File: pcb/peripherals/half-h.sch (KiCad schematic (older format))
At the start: 12 parts, among them Q201 RQ3E100BNTB, Q202 RQ3E100BNTB, U201 DGD0506A

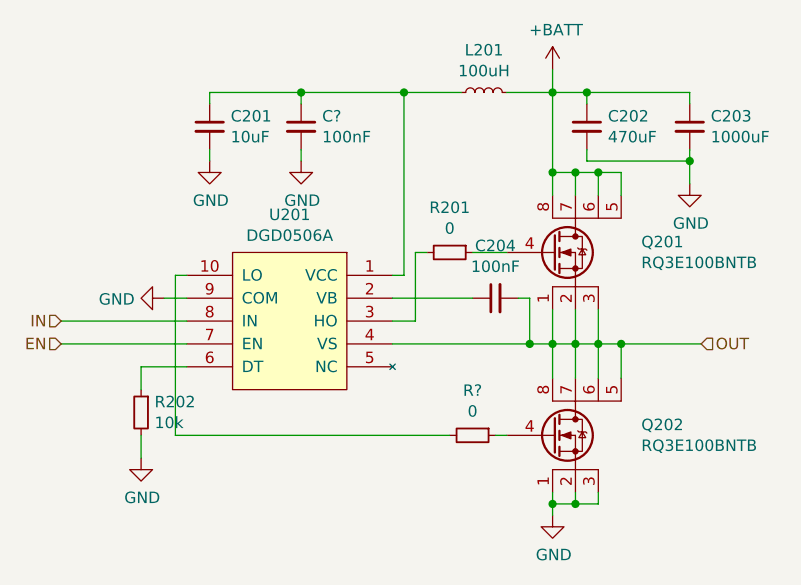
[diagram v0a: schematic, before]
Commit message: Schematic done; TODO add footprints for connectors
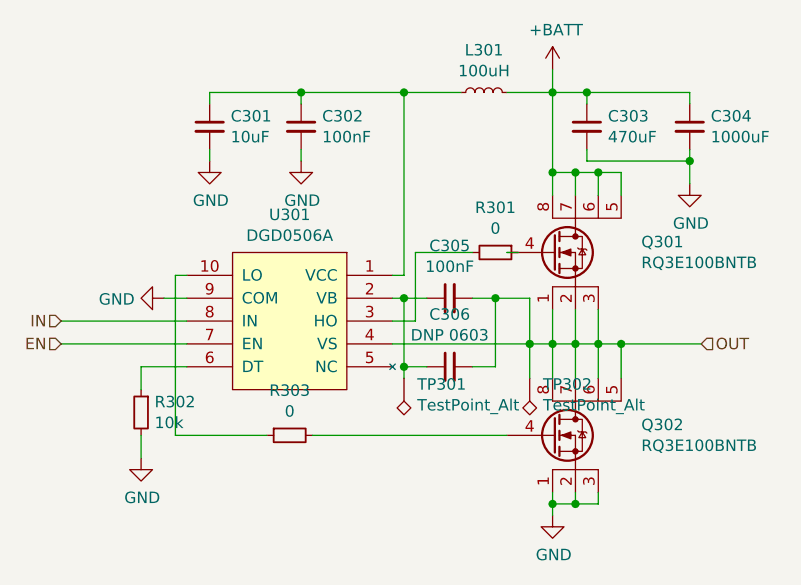
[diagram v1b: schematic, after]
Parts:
- added C206: DNP 0603, Capacitors_SMD:C_0603_HandSoldering, symbol Device:C_Small
- added TP201, TP202: TestPoint_Alt, symbol Connector:TestPoint_Alt
- C205: renamed from C204; footprint (none) -> Capacitors_SMD:C_0402; Mouser (none) -> 710-885012105018
- gave numbers to parts that had none: 2
- renumbered C202 to C203, C203 to C204
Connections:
- net OUT: now also C206.2, TP202.1
- net at U201.10 (LO): now also R203.1; no longer R203.2
- net at C205.1, U201.2 (VB): now also C206.1, TP201.1
- net at Q202.4 (G): now also R203.2; no longer R203.1
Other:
- moved on the sheet: C305, R301, R303

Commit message: Save before autofill
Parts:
- TP201: footprint (none) -> Measurement_Points:Measurement_Point_Round-SMD-Pad_Small; Mouser (none) -> NoPart
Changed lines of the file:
@@
 $Descr A4 11693 8268
 encoding utf-8
-Sheet 3 9
+Sheet 2 9
 Title ""
 Date ""
@@
 AR Path="/5B6E6A6C/5B7233C9" Ref="Q801"  Part="1"
 AR Path="/5B6E6A71/5B7233C9" Ref="Q901"  Part="1"
-F 0 "Q301" H 5788 3146 50  0000 L CNN
+F 0 "Q201" H 5788 3146 50  0000 L CNN
 F 1 "RQ3E100BNTB" H 5788 3055 50  0000 L CNN
 F 2 "peripherals:Rohm-HSMT8" H 5600 3200 50  0001 C CNN
@@
 AR Path="/5B6E6A6C/5B7233D1" Ref="U801"  Part="1"
 AR Path="/5B6E6A71/5B7233D1" Ref="U901"  Part="1"
-F 0 "U301" H 4250 3865 50  0000 C CNN
+F 0 "U201" H 4250 3865 50  0000 C CNN
 F 1 "DGD0506A" H 4250 3774 50  0000 C CNN
 F 2 "peripherals:Diodes-MSOP10" H 4250 3800 50  0001 C CNN
@@
 AR Path="/5B6E6A6C/5B7233E5" Ref="#PWR0807"  Part="1"
 AR Path="/5B6E6A71/5B7233E5" Ref="#PWR0907"  Part="1"
-F 0 "#PWR0307" H 5400 4000 50  0001 C CNN
+F 0 "#PWR0207" H 5400 4000 50  0001 C CNN
 F 1 "GND" H 5405 4077 50  0000 C CNN
 F 2 "" H 5400 4250 50  0001 C CNN
@@
 AR Path="/5B6E6A6C/5B7233F3" Ref="R801"  Part="1"
 AR Path="/5B6E6A71/5B7233F3" Ref="R901"  Part="1"
-F 0 "R301" V 4954 3100 50  0000 C CNN
+F 0 "R201" V 4954 3100 50  0000 C CNN
 F 1 "0" V 5045 3100 50  0000 C CNN
 F 2 "Resistors_SMD:R_0603_HandSoldering" H 5150 3100 50  0001 C CNN
@@
 AR Path="/5B6E6A6C/5B723403" Ref="#PWR0805"  Part="1"
 AR Path="/5B6E6A71/5B723403" Ref="#PWR0905"  Part="1"
-F 0 "#PWR0305" H 3700 3050 50  0001 C CNN
+F 0 "#PWR0205" H 3700 3050 50  0001 C CNN
 F 1 "GND" V 3705 3172 50  0000 R CNN
 F 2 "" H 3700 3300 50  0001 C CNN
@@
 AR Path="/5B6E6A6C/5B723409" Ref="R802"  Part="1"
 AR Path="/5B6E6A71/5B723409" Ref="R902"  Part="1"
-F 0 "R302" H 3541 3846 50  0000 R CNN
+F 0 "R202" H 3541 3846 50  0000 R CNN
 F 1 "10k" H 3541 3755 50  0000 R CNN
 F 2 "Resistors_SMD:R_0402" H 3600 3800 50  0001 C CNN
@@
 AR Path="/5B6E6A6C/5B723410" Ref="#PWR0806"  Part="1"
 AR Path="/5B6E6A71/5B723410" Ref="#PWR0906"  Part="1"
-F 0 "#PWR0306" H 3600 3750 50  0001 C CNN
+F 0 "#PWR0206" H 3600 3750 50  0001 C CNN
 F 1 "GND" H 3605 3827 50  0000 C CNN
 F 2 "" H 3600 4000 50  0001 C CNN
@@
 AR Path="/5B6E6A6C/5B723429" Ref="C805"  Part="1"
 AR Path="/5B6E6A71/5B723429" Ref="C905"  Part="1"
-F 0 "C305" V 4721 3300 50  0000 C CNN
+F 0 "C205" V 4721 3300 50  0000 C CNN
 F 1 "100nF" V 4812 3300 50  0000 C CNN
 F 2 "Capacitors_SMD:C_0402" H 4950 3300 50  0001 C CNN
@@
 AR Path="/5B6E6A6C/5B723443" Ref="C801"  Part="1"
 AR Path="/5B6E6A71/5B723443" Ref="C901"  Part="1"
-F 0 "C301" H 3992 2596 50  0000 L CNN
+F 0 "C201" H 3992 2596 50  0000 L CNN
 F 1 "10uF" H 3992 2505 50  0000 L CNN
 F 2 "Capacitors_SMD:CP_Elec_4x5.7" H 3900 2550 50  0001 C CNN
@@
 AR Path="/5B6E6A6C/5B72344C" Ref="#PWR0803"  Part="1"
 AR Path="/5B6E6A71/5B72344C" Ref="#PWR0903"  Part="1"
-F 0 "#PWR0303" H 4300 2450 50  0001 C CNN
+F 0 "#PWR0203" H 4300 2450 50  0001 C CNN
 F 1 "GND" H 4305 2527 50  0000 C CNN
 F 2 "" H 4300 2700 50  0001 C CNN
@@
 AR Path="/5B6E6A6C/5B723454" Ref="C803"  Part="1"
 AR Path="/5B6E6A71/5B723454" Ref="C903"  Part="1"
-F 0 "C303" H 5642 2596 50  0000 L CNN
+F 0 "C203" H 5642 2596 50  0000 L CNN
 F 1 "470uF" H 5642 2505 50  0000 L CNN
 F 2 "Capacitors_ThroughHole:CP_Radial_D10.0mm_P5.00mm" H 5550 2550 50  0001 C CNN
@@
 AR Path="/5B6E6A6C/5B72345C" Ref="C804"  Part="1"
 AR Path="/5B6E6A71/5B72345C" Ref="C904"  Part="1"
-F 0 "C304" H 6092 2596 50  0000 L CNN
+F 0 "C204" H 6092 2596 50  0000 L CNN
 F 1 "1000uF" H 6092 2505 50  0000 L CNN
 F 2 "Capacitors_ThroughHole:CP_Radial_D18.0mm_P7.50mm" H 6000 2550 50  0001 C CNN
@@
 AR Path="/5B6E6A6C/5B723466" Ref="#PWR0804"  Part="1"
 AR Path="/5B6E6A71/5B723466" Ref="#PWR0904"  Part="1"
-F 0 "#PWR0304" H 6000 2550 50  0001 C CNN
+F 0 "#PWR0204" H 6000 2550 50  0001 C CNN
 F 1 "GND" H 6005 2627 50  0000 C CNN
 F 2 "" H 6000 2800 50  0001 C CNN
@@
 AR Path="/5B6E6A6C/5B723472" Ref="L801"  Part="1"
 AR Path="/5B6E6A71/5B723472" Ref="L901"  Part="1"
-F 0 "L301" V 5285 2400 50  0000 C CNN
+F 0 "L201" V 5285 2400 50  0000 C CNN
 F 1 "100uH" V 5194 2400 50  0000 C CNN
 F 2 "Resistors_SMD:R_0805_HandSoldering" H 5100 2400 50  0001 C CNN
@@
 AR Path="/5B6E6A6C/5B72347E" Ref="#PWR0801"  Part="1"
 AR Path="/5B6E6A71/5B72347E" Ref="#PWR0901"  Part="1"
-F 0 "#PWR0301" H 5400 2150 50  0001 C CNN
+F 0 "#PWR0201" H 5400 2150 50  0001 C CNN
 F 1 "+BATT" H 5415 2473 50  0000 C CNN
 F 2 "" H 5400 2300 50  0001 C CNN
@@
 AR Path="/5B6E6A6C/5B723489" Ref="Q802"  Part="1"
 AR Path="/5B6E6A71/5B723489" Ref="Q902"  Part="1"
-F 0 "Q302" H 5788 3946 50  0000 L CNN
+F 0 "Q202" H 5788 3946 50  0000 L CNN
 F 1 "RQ3E100BNTB" H 5788 3855 50  0000 L CNN
 F 2 "peripherals:Rohm-HSMT8" H 5600 4000 50  0001 C CNN
@@
 AR Path="/5B6E6A6C/5B727333" Ref="R803"  Part="1"
 AR Path="/5B6E6A71/5B727333" Ref="R903"  Part="1"
-F 0 "R303" V 4054 3900 50  0000 C CNN
+F 0 "R203" V 4054 3900 50  0000 C CNN
 F 1 "0" V 4145 3900 50  0000 C CNN
 F 2 "Resistors_SMD:R_0603_HandSoldering" H 4250 3900 50  0001 C CNN
@@
 AR Path="/5B6E6A6C/5B728A25" Ref="#PWR0802"  Part="1"
 AR Path="/5B6E6A71/5B728A25" Ref="#PWR0902"  Part="1"
-F 0 "#PWR0302" H 3900 2450 50  0001 C CNN
+F 0 "#PWR0202" H 3900 2450 50  0001 C CNN
 F 1 "GND" H 3905 2527 50  0000 C CNN
 F 2 "" H 3900 2700 50  0001 C CNN
@@
 AR Path="/5B6E6A6C/5B72F72D" Ref="C802"  Part="1"
 AR Path="/5B6E6A71/5B72F72D" Ref="C902"  Part="1"
-F 0 "C302" H 4392 2596 50  0000 L CNN
+F 0 "C202" H 4392 2596 50  0000 L CNN
 F 1 "100nF" H 4392 2505 50  0000 L CNN
 F 2 "Capacitors_SMD:C_0402" H 4300 2550 50  0001 C CNN
@@
 AR Path="/5B6E6A6C/5B6EFABB" Ref="C806"  Part="1"
 AR Path="/5B6E6A71/5B6EFABB" Ref="C906"  Part="1"
-F 0 "C306" V 4721 3600 50  0000 C CNN
+F 0 "C206" V 4721 3600 50  0000 C CNN
 F 1 "DNP 0603" V 4812 3600 50  0000 C CNN
 F 2 "Capacitors_SMD:C_0603_HandSoldering" H 4950 3600 50  0001 C CNN
@@
 AR Path="/5B6E6A6C/5B6F8326" Ref="TP801"  Part="1"
 AR Path="/5B6E6A71/5B6F8326" Ref="TP901"  Part="1"
-F 0 "TP301" H 4692 3677 50  0000 R CNN
+F 0 "TP201" H 4692 3677 50  0000 R CNN
 F 1 "TestPoint_Alt" H 4692 3768 50  0000 R CNN
-F 2 "" H 4950 3650 50  0001 C CNN
+F 2 "Measurement_Points:Measurement_Point_Round-SMD-Pad_Small" H 4950 3650 50  0001 C CNN
 F 3 "~" H 4950 3650 50  0001 C CNN
+F 4 "NoPart" H 4750 3650 50  0001 C CNN "Mouser"
 	1    4750 3650
 	-1   0    0    1
@@
 AR Path="/5B6E6A6C/5B6F99EB" Ref="TP802"  Part="1"
 AR Path="/5B6E6A71/5B6F99EB" Ref="TP902"  Part="1"
-F 0 "TP302" H 5242 3677 50  0000 R CNN
+F 0 "TP202" H 5242 3677 50  0000 R CNN
 F 1 "TestPoint_Alt" H 5242 3768 50  0000 R CNN
 F 2 "" H 5500 3650 50  0001 C CNN

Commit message: Save before messing with tiler script
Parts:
- TP202: footprint (none) -> Measurement_Points:Measurement_Point_Round-SMD-Pad_Small; Mouser (none) -> NoPart
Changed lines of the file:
@@
 AR Path="/5B6E6A6C/5B7233C9" Ref="Q801"  Part="1"
 AR Path="/5B6E6A71/5B7233C9" Ref="Q901"  Part="1"
-F 0 "Q201" H 5788 3146 50  0000 L CNN
+F 0 "Q301" H 5788 3146 50  0000 L CNN
 F 1 "RQ3E100BNTB" H 5788 3055 50  0000 L CNN
 F 2 "peripherals:Rohm-HSMT8" H 5600 3200 50  0001 C CNN
@@
 AR Path="/5B6E6A6C/5B7233D1" Ref="U801"  Part="1"
 AR Path="/5B6E6A71/5B7233D1" Ref="U901"  Part="1"
-F 0 "U201" H 4250 3865 50  0000 C CNN
+F 0 "U301" H 4250 3865 50  0000 C CNN
 F 1 "DGD0506A" H 4250 3774 50  0000 C CNN
 F 2 "peripherals:Diodes-MSOP10" H 4250 3800 50  0001 C CNN
@@
 AR Path="/5B6E6A6C/5B7233E5" Ref="#PWR0807"  Part="1"
 AR Path="/5B6E6A71/5B7233E5" Ref="#PWR0907"  Part="1"
-F 0 "#PWR0207" H 5400 4000 50  0001 C CNN
+F 0 "#PWR0307" H 5400 4000 50  0001 C CNN
 F 1 "GND" H 5405 4077 50  0000 C CNN
 F 2 "" H 5400 4250 50  0001 C CNN
@@
 AR Path="/5B6E6A6C/5B7233F3" Ref="R801"  Part="1"
 AR Path="/5B6E6A71/5B7233F3" Ref="R901"  Part="1"
-F 0 "R201" V 4954 3100 50  0000 C CNN
+F 0 "R301" V 4954 3100 50  0000 C CNN
 F 1 "0" V 5045 3100 50  0000 C CNN
 F 2 "Resistors_SMD:R_0603_HandSoldering" H 5150 3100 50  0001 C CNN
@@
 AR Path="/5B6E6A6C/5B723403" Ref="#PWR0805"  Part="1"
 AR Path="/5B6E6A71/5B723403" Ref="#PWR0905"  Part="1"
-F 0 "#PWR0205" H 3700 3050 50  0001 C CNN
+F 0 "#PWR0305" H 3700 3050 50  0001 C CNN
 F 1 "GND" V 3705 3172 50  0000 R CNN
 F 2 "" H 3700 3300 50  0001 C CNN
@@
 AR Path="/5B6E6A6C/5B723409" Ref="R802"  Part="1"
 AR Path="/5B6E6A71/5B723409" Ref="R902"  Part="1"
-F 0 "R202" H 3541 3846 50  0000 R CNN
+F 0 "R302" H 3541 3846 50  0000 R CNN
 F 1 "10k" H 3541 3755 50  0000 R CNN
 F 2 "Resistors_SMD:R_0402" H 3600 3800 50  0001 C CNN
@@
 AR Path="/5B6E6A6C/5B723410" Ref="#PWR0806"  Part="1"
 AR Path="/5B6E6A71/5B723410" Ref="#PWR0906"  Part="1"
-F 0 "#PWR0206" H 3600 3750 50  0001 C CNN
+F 0 "#PWR0306" H 3600 3750 50  0001 C CNN
 F 1 "GND" H 3605 3827 50  0000 C CNN
 F 2 "" H 3600 4000 50  0001 C CNN
@@
 AR Path="/5B6E6A6C/5B723429" Ref="C805"  Part="1"
 AR Path="/5B6E6A71/5B723429" Ref="C905"  Part="1"
-F 0 "C205" V 4721 3300 50  0000 C CNN
+F 0 "C305" V 4721 3300 50  0000 C CNN
 F 1 "100nF" V 4812 3300 50  0000 C CNN
 F 2 "Capacitors_SMD:C_0402" H 4950 3300 50  0001 C CNN
@@
 	4750 3200 4700 3200
 Wire Wire Line
-	6050 3500 5700 3500
+	6050 3500 5900 3500
 Connection ~ 5700 3500
 Wire Wire Line
@@
 AR Path="/5B6E6A6C/5B723443" Ref="C801"  Part="1"
 AR Path="/5B6E6A71/5B723443" Ref="C901"  Part="1"
-F 0 "C201" H 3992 2596 50  0000 L CNN
+F 0 "C301" H 3992 2596 50  0000 L CNN
 F 1 "10uF" H 3992 2505 50  0000 L CNN
 F 2 "Capacitors_SMD:CP_Elec_4x5.7" H 3900 2550 50  0001 C CNN
@@
 AR Path="/5B6E6A6C/5B72344C" Ref="#PWR0803"  Part="1"
 AR Path="/5B6E6A71/5B72344C" Ref="#PWR0903"  Part="1"
-F 0 "#PWR0203" H 4300 2450 50  0001 C CNN
+F 0 "#PWR0303" H 4300 2450 50  0001 C CNN
 F 1 "GND" H 4305 2527 50  0000 C CNN
 F 2 "" H 4300 2700 50  0001 C CNN
@@
 AR Path="/5B6E6A6C/5B723454" Ref="C803"  Part="1"
 AR Path="/5B6E6A71/5B723454" Ref="C903"  Part="1"
-F 0 "C203" H 5642 2596 50  0000 L CNN
+F 0 "C303" H 5642 2596 50  0000 L CNN
 F 1 "470uF" H 5642 2505 50  0000 L CNN
 F 2 "Capacitors_ThroughHole:CP_Radial_D10.0mm_P5.00mm" H 5550 2550 50  0001 C CNN
@@
 AR Path="/5B6E6A6C/5B72345C" Ref="C804"  Part="1"
 AR Path="/5B6E6A71/5B72345C" Ref="C904"  Part="1"
-F 0 "C204" H 6092 2596 50  0000 L CNN
+F 0 "C304" H 6092 2596 50  0000 L CNN
 F 1 "1000uF" H 6092 2505 50  0000 L CNN
 F 2 "Capacitors_ThroughHole:CP_Radial_D18.0mm_P7.50mm" H 6000 2550 50  0001 C CNN
@@
 AR Path="/5B6E6A6C/5B723466" Ref="#PWR0804"  Part="1"
 AR Path="/5B6E6A71/5B723466" Ref="#PWR0904"  Part="1"
-F 0 "#PWR0204" H 6000 2550 50  0001 C CNN
+F 0 "#PWR0304" H 6000 2550 50  0001 C CNN
 F 1 "GND" H 6005 2627 50  0000 C CNN
 F 2 "" H 6000 2800 50  0001 C CNN
@@
 AR Path="/5B6E6A6C/5B723472" Ref="L801"  Part="1"
 AR Path="/5B6E6A71/5B723472" Ref="L901"  Part="1"
-F 0 "L201" V 5285 2400 50  0000 C CNN
+F 0 "L301" V 5285 2400 50  0000 C CNN
 F 1 "100uH" V 5194 2400 50  0000 C CNN
 F 2 "Resistors_SMD:R_0805_HandSoldering" H 5100 2400 50  0001 C CNN
@@
 AR Path="/5B6E6A6C/5B72347E" Ref="#PWR0801"  Part="1"
 AR Path="/5B6E6A71/5B72347E" Ref="#PWR0901"  Part="1"
-F 0 "#PWR0201" H 5400 2150 50  0001 C CNN
+F 0 "#PWR0301" H 5400 2150 50  0001 C CNN
 F 1 "+BATT" H 5415 2473 50  0000 C CNN
 F 2 "" H 5400 2300 50  0001 C CNN
@@
 AR Path="/5B6E6A6C/5B723489" Ref="Q802"  Part="1"
 AR Path="/5B6E6A71/5B723489" Ref="Q902"  Part="1"
-F 0 "Q202" H 5788 3946 50  0000 L CNN
+F 0 "Q302" H 5788 3946 50  0000 L CNN
 F 1 "RQ3E100BNTB" H 5788 3855 50  0000 L CNN
 F 2 "peripherals:Rohm-HSMT8" H 5600 4000 50  0001 C CNN
@@
 AR Path="/5B6E6A6C/5B727333" Ref="R803"  Part="1"
 AR Path="/5B6E6A71/5B727333" Ref="R903"  Part="1"
-F 0 "R203" V 4054 3900 50  0000 C CNN
+F 0 "R303" V 4054 3900 50  0000 C CNN
 F 1 "0" V 4145 3900 50  0000 C CNN
 F 2 "Resistors_SMD:R_0603_HandSoldering" H 4250 3900 50  0001 C CNN
@@
 AR Path="/5B6E6A6C/5B728A25" Ref="#PWR0802"  Part="1"
 AR Path="/5B6E6A71/5B728A25" Ref="#PWR0902"  Part="1"
-F 0 "#PWR0202" H 3900 2450 50  0001 C CNN
+F 0 "#PWR0302" H 3900 2450 50  0001 C CNN
 F 1 "GND" H 3905 2527 50  0000 C CNN
 F 2 "" H 3900 2700 50  0001 C CNN
@@
 AR Path="/5B6E6A6C/5B72F72D" Ref="C802"  Part="1"
 AR Path="/5B6E6A71/5B72F72D" Ref="C902"  Part="1"
-F 0 "C202" H 4392 2596 50  0000 L CNN
+F 0 "C302" H 4392 2596 50  0000 L CNN
 F 1 "100nF" H 4392 2505 50  0000 L CNN
 F 2 "Capacitors_SMD:C_0402" H 4300 2550 50  0001 C CNN
@@
 AR Path="/5B6E6A6C/5B6EFABB" Ref="C806"  Part="1"
 AR Path="/5B6E6A71/5B6EFABB" Ref="C906"  Part="1"
-F 0 "C206" V 4721 3600 50  0000 C CNN
+F 0 "C306" V 4721 3600 50  0000 C CNN
 F 1 "DNP 0603" V 4812 3600 50  0000 C CNN
 F 2 "Capacitors_SMD:C_0603_HandSoldering" H 4950 3600 50  0001 C CNN
@@
 AR Path="/5B6E6A6C/5B6F8326" Ref="TP801"  Part="1"
 AR Path="/5B6E6A71/5B6F8326" Ref="TP901"  Part="1"
-F 0 "TP201" H 4692 3677 50  0000 R CNN
+F 0 "TP301" H 4692 3677 50  0000 R CNN
 F 1 "TestPoint_Alt" H 4692 3768 50  0000 R CNN
 F 2 "Measurement_Points:Measurement_Point_Round-SMD-Pad_Small" H 4950 3650 50  0001 C CNN
@@
 AR Path="/5B6E6A6C/5B6F99EB" Ref="TP802"  Part="1"
 AR Path="/5B6E6A71/5B6F99EB" Ref="TP902"  Part="1"
-F 0 "TP202" H 5242 3677 50  0000 R CNN
+F 0 "TP302" H 5242 3677 50  0000 R CNN
 F 1 "TestPoint_Alt" H 5242 3768 50  0000 R CNN
-F 2 "" H 5500 3650 50  0001 C CNN
+F 2 "Measurement_Points:Measurement_Point_Round-SMD-Pad_Small" H 5500 3650 50  0001 C CNN
 F 3 "~" H 5500 3650 50  0001 C CNN
+F 4 "NoPart" H 5500 3650 50  0001 C CNN "Mouser"
 	1    5300 3650
 	-1   0    0    1
@@
 Wire Wire Line
 	5300 3500 5300 3650
+$Comp
+L power:PWR_FLAG #FLG0103
+U 1 1 5B6F59A4
+P 4750 2300
+AR Path="/5B7230C4/5B6F59A4" Ref="#FLG0103"  Part="1"
+AR Path="/5B6E69BA/5B6F59A4" Ref="#FLG0104"  Part="1"
+AR Path="/5B6E69C9/5B6F59A4" Ref="#FLG0105"  Part="1"
+AR Path="/5B6E69CE/5B6F59A4" Ref="#FLG0106"  Part="1"
+AR Path="/5B6E6A62/5B6F59A4" Ref="#FLG0107"  Part="1"
+AR Path="/5B6E6A67/5B6F59A4" Ref="#FLG0108"  Part="1"
+AR Path="/5B6E6A6C/5B6F59A4" Ref="#FLG0109"  Part="1"
+AR Path="/5B6E6A71/5B6F59A4" Ref="#FLG0110"  Part="1"
+F 0 "#FLG0104" H 4750 2375 50  0001 C CNN
+F 1 "PWR_FLAG" H 4750 2474 50  0000 C CNN
+F 2 "" H 4750 2300 50  0001 C CNN
+F 3 "~" H 4750 2300 50  0001 C CNN
+	1    4750 2300
+	1    0    0    -1
+$EndComp
+Wire Wire Line
+	4750 2300 4750 2400
+$Comp
+L power:PWR_FLAG #FLG0111
+U 1 1 5B6F73EE
+P 5900 3450
+AR Path="/5B7230C4/5B6F73EE" Ref="#FLG0111"  Part="1"
+AR Path="/5B6E69BA/5B6F73EE" Ref="#FLG0112"  Part="1"
+AR Path="/5B6E69C9/5B6F73EE" Ref="#FLG0113"  Part="1"
+AR Path="/5B6E69CE/5B6F73EE" Ref="#FLG0114"  Part="1"
+AR Path="/5B6E6A62/5B6F73EE" Ref="#FLG0115"  Part="1"
+AR Path="/5B6E6A67/5B6F73EE" Ref="#FLG0116"  Part="1"
+AR Path="/5B6E6A6C/5B6F73EE" Ref="#FLG0117"  Part="1"
+AR Path="/5B6E6A71/5B6F73EE" Ref="#FLG0118"  Part="1"
+F 0 "#FLG0112" H 5900 3525 50  0001 C CNN
+F 1 "PWR_FLAG" H 5900 3624 50  0000 C CNN
+F 2 "" H 5900 3450 50  0001 C CNN
+F 3 "~" H 5900 3450 50  0001 C CNN
+	1    5900 3450
+	1    0    0    -1
+$EndComp
+Wire Wire Line
+	5900 3450 5900 3500
+Connection ~ 5900 3500
+Wire Wire Line
+	5900 3500 5700 3500
 $EndSCHEMATC
